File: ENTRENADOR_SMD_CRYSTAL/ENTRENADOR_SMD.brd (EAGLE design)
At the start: 99.8 x 100.2 mm, 95 parts, among them IC1 PIC16F1939PT, IC2 7824T, J1 DCJ0202, SW1 TL3342F160QG/TR, Y1 ABLS2-4.096MHZ-D4Y-T

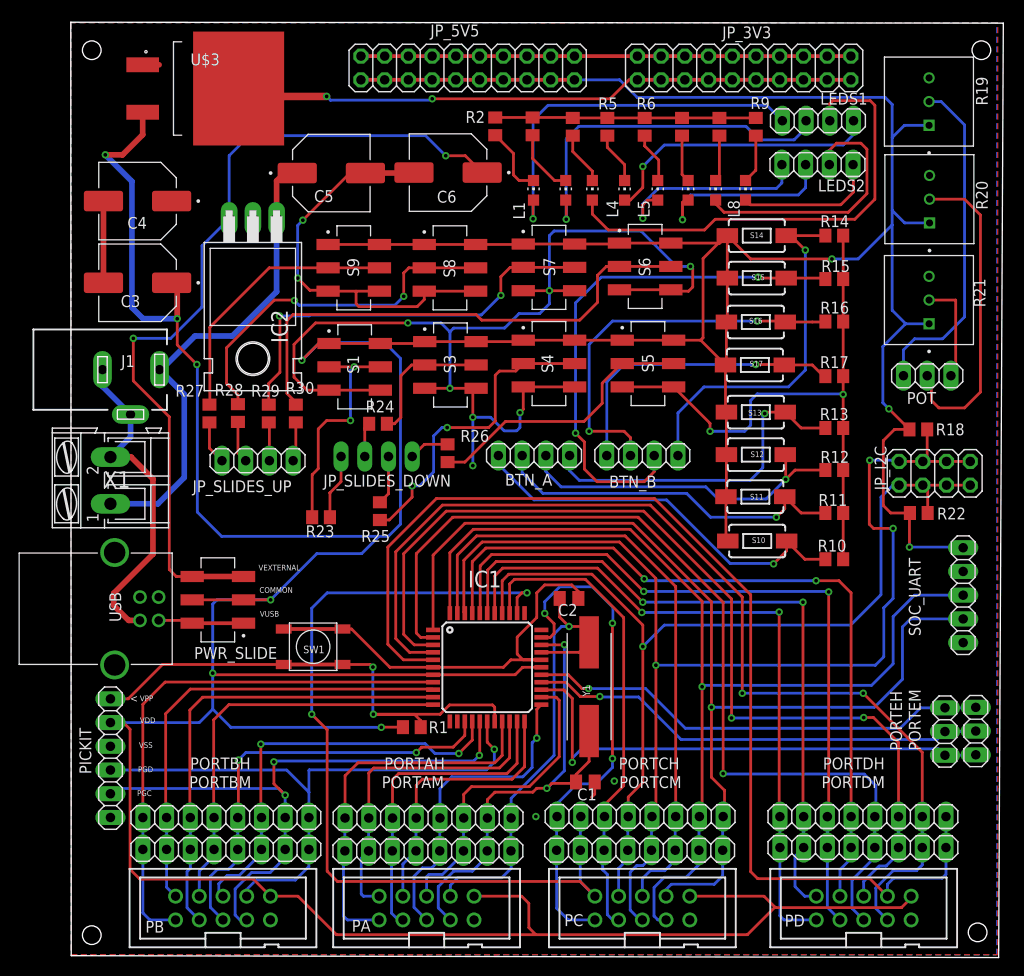
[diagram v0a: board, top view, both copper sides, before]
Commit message: Se ajusta el PCB SMD en perforacion
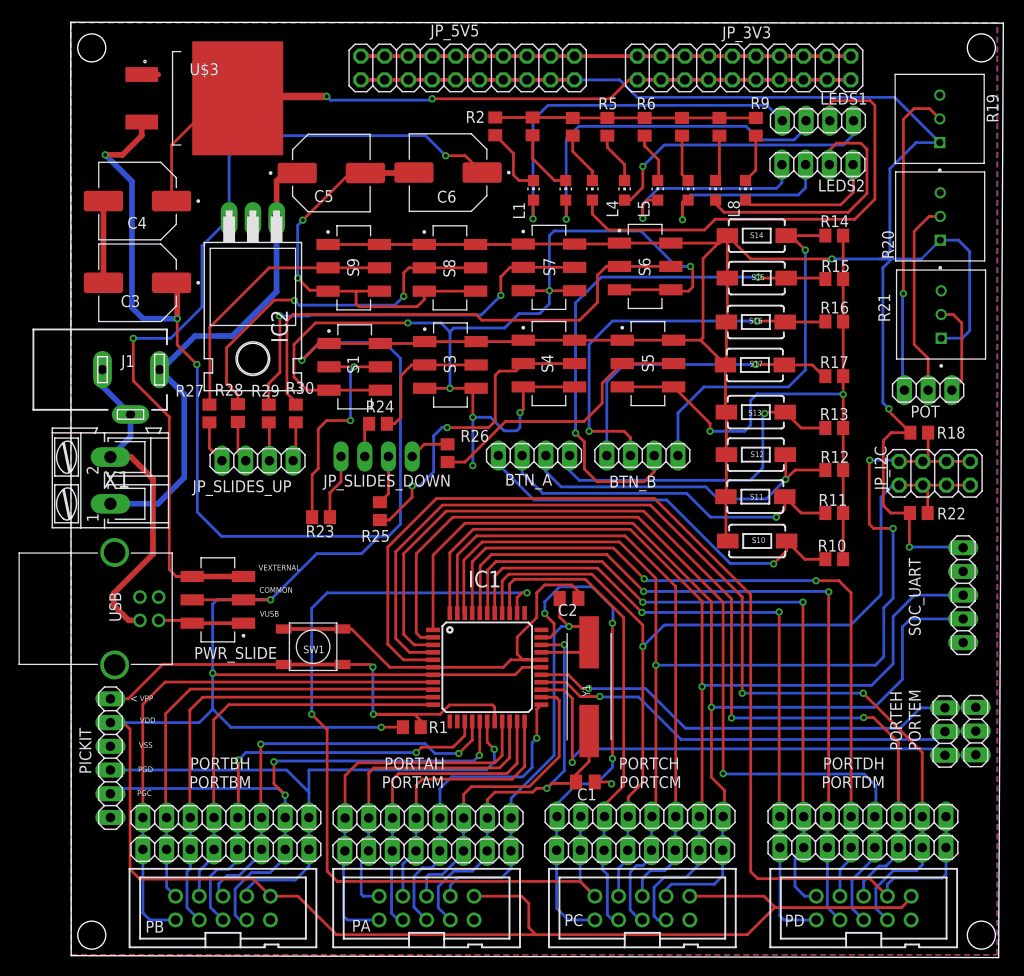
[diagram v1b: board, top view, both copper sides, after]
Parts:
- moved R19 2.18 mm to (93.0, 89.7)
- moved R20 2.18 mm to (93.1, 79.2)
- moved R21 2.02 mm to (93.2, 68.7)
- moved POT 1.55 mm to (91.8, 60.6)
- moved U$3 1.05 mm to (14.3, 91.8)
- moved R18 0.36 mm to (90.8, 56.0)
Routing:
- net VCC: track 627.9 -> 641.1 mm
- net N$34: track 34.2 -> 21.1 mm
- net 3V3: track 72.1 -> 83.5 mm
- net N$35: track 36.2 -> 34.0 mm, vias 0 -> 1
- net N$33: track 11.2 -> 10.2 mm
- net GND: vias 13 -> 12
